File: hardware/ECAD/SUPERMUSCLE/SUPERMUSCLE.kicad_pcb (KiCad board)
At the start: 2 copper layers, 83 x 96 mm, 50 parts, among them J1 Conn_01x02_Male, J10 Conn_01x16_Male, J11 Conn_01x05, J12 Conn_Coaxial_Power, J2 Conn_01x02_Male, J3 Conn_01x02_Male, J4 Conn_01x02_Male, J5 Conn_01x02_Male, J6 Conn_01x02_Male, J7 Conn_01x02_Male, J8 Conn_01x02_Male, J9 Conn_01x05, SW1 RotaryEncoder_Switch, SW2 SW_DIP_x01, U1 Teensy4.1, U2 6N138

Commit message: hardware update
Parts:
- added R29: 10K, Resistor_THT:R_Axial_DIN0204_L3.6mm_D1.6mm_P5.08mm_Horizontal, F.Cu at (113.2, 53.1)
- U2: footprint Package_DIP:DIP-14_W7.62mm_Socket_LongPads -> Package_DIP:DIP-8_W7.62mm_Socket_LongPads
- moved U2 3.71 mm to (120.8, 41.9)
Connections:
- U2 pad 7: unconnected-(U2-Pad7) -> Net-(U2-Pad7)
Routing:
- net +5V: track 164.7 -> 176.0 mm
- net GND: track 309.1 -> 301.8 mm
- net Net-(R27-Pad1): track 54.7 -> 59.6 mm
- net Net-(U2-Pad7): track 0.00 -> 3.59 mm
- net Net-(D1-Pad2): track 22.6 -> 25.7 mm
- net Net-(D1-Pad1): track 9.82 -> 12.3 mm
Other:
- board text added: "2"
- board text added: "4"
- board text added: "5"
- board text added: "SUPER MUSCLE v.1.1"
- board text removed: "SUPER MUSCLE v.1.0"

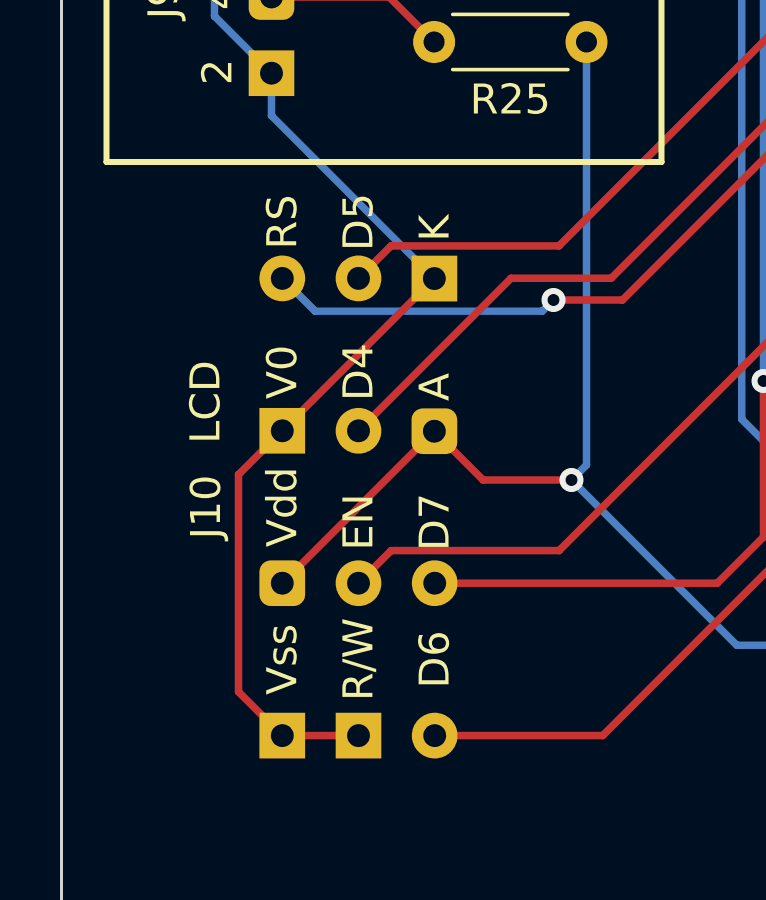
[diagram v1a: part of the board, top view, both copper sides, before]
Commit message: pcb + code annotations
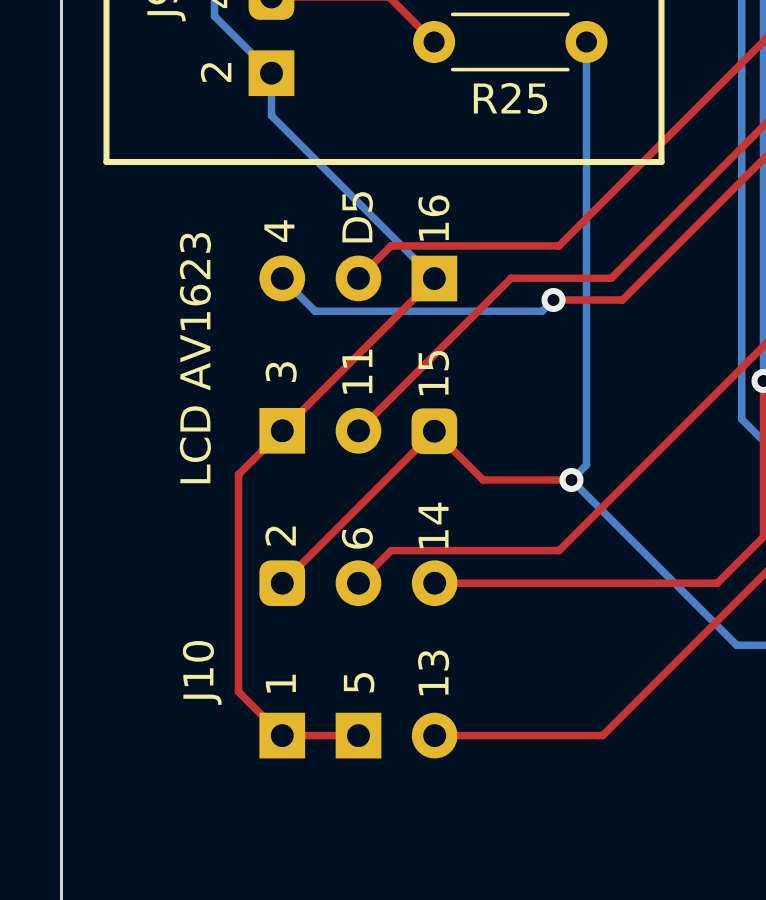
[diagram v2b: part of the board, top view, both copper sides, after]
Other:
- board text added: "LCD AV1623"
- board text removed: "LCD"
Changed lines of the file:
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@@
     (property "Sheetname" "")
     (attr through_hole)
-    (fp_text reference "J10" (at 0 -2.54 90 unlocked) (layer "F.SilkS")
-      (effects (font (size 1 1) (thickness 0.15)))
-    )
-    (fp_text value "Conn_01x16_Male" (at 0 5.08 90 unlocked) (layer "F.Fab")
-      (effects (font (size 1 1) (thickness 0.15)))
-    )
-    (fp_text user "V0" (at 4.5 0 90 unlocked) (layer "F.SilkS")
-      (effects (font (size 1 1) (thickness 0.15)))
-    )
-    (fp_text user "Vss" (at -5.08 0 90 unlocked) (layer "F.SilkS")
-      (effects (font (size 1 1) (thickness 0.15)))
-    )
-    (fp_text user "Vdd" (at 0 0 90 unlocked) (layer "F.SilkS")
-      (effects (font (size 1 1) (thickness 0.15)))
-    )
-    (fp_text user "EN" (at -0.5 2.54 90 unlocked) (layer "F.SilkS")
-      (effects (font (size 1 1) (thickness 0.15)))
-    )
-    (fp_text user "A" (at 4 5.08 90 unlocked) (layer "F.SilkS")
-      (effects (font (size 1 1) (thickness 0.15)))
-    )
-    (fp_text user "RS" (at 9.5 0 90 unlocked) (layer "F.SilkS")
-      (effects (font (size 1 1) (thickness 0.15)))
-    )
-    (fp_text user "R/W" (at -5.08 2.54 90 unlocked) (layer "F.SilkS")
-      (effects (font (size 1 1) (thickness 0.15)))
-    )
-    (fp_text user "D5" (at 9.5 2.54 90 unlocked) (layer "F.SilkS")
-      (effects (font (size 1 1) (thickness 0.15)))
-    )
-    (fp_text user "K" (at 9.3 5.08 90 unlocked) (layer "F.SilkS")
-      (effects (font (size 1 1) (thickness 0.15)))
-    )
-    (fp_text user "D7" (at -0.5 5.08 90 unlocked) (layer "F.SilkS")
-      (effects (font (size 1 1) (thickness 0.15)))
-    )
-    (fp_text user "D4" (at 4.5 2.54 90 unlocked) (layer "F.SilkS")
-      (effects (font (size 1 1) (thickness 0.15)))
-    )
-    (fp_text user "D6" (at -5.08 5.08 90 unlocked) (layer "F.SilkS")
+    (fp_text reference "J10" (at -5.45 -2.76 90 unlocked) (layer "F.SilkS")
+      (effects (font (size 1 1) (thickness 0.15)))
+    )
+    (fp_text value "Conn_01x16_Male" (at 0 6.79 90 unlocked) (layer "F.Fab")
+      (effects (font (size 1 1) (thickness 0.15)))
+    )
+    (fp_text user "3" (at 4.5 0 90 unlocked) (layer "F.SilkS")
+      (effects (font (size 1 1) (thickness 0.15)))
+    )
+    (fp_text user "1" (at -5.9 -0.01 90 unlocked) (layer "F.SilkS")
+      (effects (font (size 1 1) (thickness 0.15)))
+    )
+    (fp_text user "2" (at -0.95 -0.01 90 unlocked) (layer "F.SilkS")
+      (effects (font (size 1 1) (thickness 0.15)))
+    )
+    (fp_text user "6" (at -1.05 2.54 90 unlocked) (layer "F.SilkS")
+      (effects (font (size 1 1) (thickness 0.15)))
+    )
+    (fp_text user "15" (at 4.45 5.08 90 unlocked) (layer "F.SilkS")
+      (effects (font (size 1 1) (thickness 0.15)))
+    )
+    (fp_text user "4" (at 9.2 -0.06 90 unlocked) (layer "F.SilkS")
+      (effects (font (size 1 1) (thickness 0.15)))
+    )
+    (fp_text user "5" (at -5.85 2.59 90 unlocked) (layer "F.SilkS")
+      (effects (font (size 1 1) (thickness 0.15)))
+    )
+    (fp_text user "D5" (at 9.65 2.54 90 unlocked) (layer "F.SilkS")
+      (effects (font (size 1 1) (thickness 0.15)))
+    )
+    (fp_text user "16" (at 9.6 5.09 90 unlocked) (layer "F.SilkS")
+      (effects (font (size 1 1) (thickness 0.15)))
+    )
+    (fp_text user "14" (at -0.65 5.08 90 unlocked) (layer "F.SilkS")
+      (effects (font (size 1 1) (thickness 0.15)))
+    )
+    (fp_text user "11" (at 4.5 2.54 90 unlocked) (layer "F.SilkS")
+      (effects (font (size 1 1) (thickness 0.15)))
+    )
+    (fp_text user "13" (at -5.55 5.08 90 unlocked) (layer "F.SilkS")
       (effects (font (size 1 1) (thickness 0.15)))
     )
@@
     (effects (font (size 1 1) (thickness 0.2)))
   )
-  (gr_text "LCD" (at 81.3 103 90) (layer "F.SilkS")
+  (gr_text "LCD AV1623" (at 81 101.55 90) (layer "F.SilkS")
     (effects (font (size 1 1) (thickness 0.2)))
   )
